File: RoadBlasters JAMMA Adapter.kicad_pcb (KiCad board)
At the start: 2 copper layers, 112.2 x 82 mm, 44 parts, among them J101 Molex_KK-396_5273-10A_1x10_P3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, J102 Molex_KK-254_AE-6410-02A_1x02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, J103 Molex_KK-254_AE-6410-02A_1x02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, J104 Molex_KK-254_AE-6410-02A_1x02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, J105 Molex_KK-254_AE-6410-04A_1x04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, J106 Molex_KK-254_AE-6410-03A_1x03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, J108 Molex_KK-254_AE-6410-05A_1x05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, P1 10K, U1 74LS86, U2 NE555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

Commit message: 152 changed to 2a152j (reduced noise), other tweaks
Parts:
- C10: value 152 -> 2A152J
- U1: footprint Package_DIP:DIP-14_W7.62mm_Socket -> Package_DIP:DIP-14_W7.62mm
- moved C7 0.25 mm to (134.2, 99.0)
- moved C11 0.20 mm to (121.1, 77.2)
- moved U2 0.18 mm to (134.4, 82.4)
- moved U1 0.16 mm to (121.0, 82.4)
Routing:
- net +5V: track 472.7 -> 473.8 mm
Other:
- board text added: "Atari® System I JAMMA Interface, Rev. 1 for RoadBlasters®"
- board text removed: "Atari® System I JAMMA Interface for RoadBlasters®, Rev. 1"

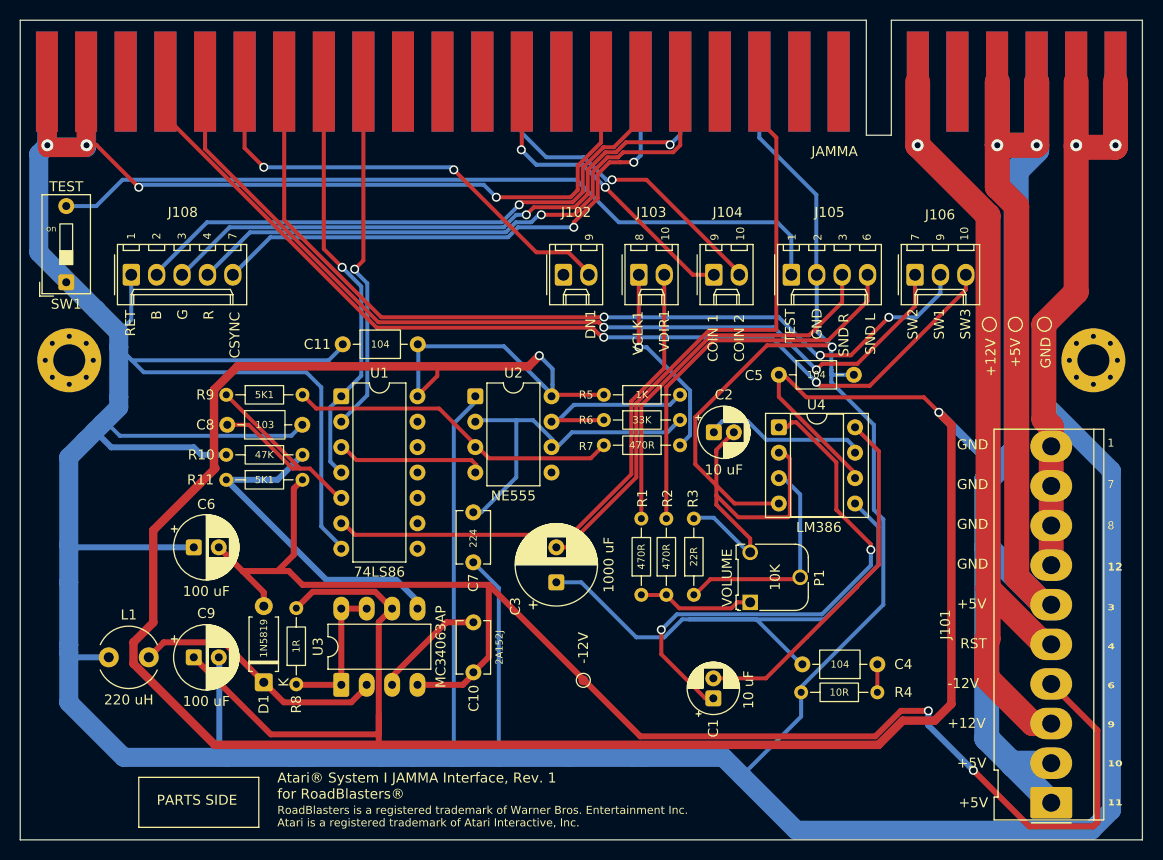
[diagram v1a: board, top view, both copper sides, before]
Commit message: add jumper to select button 2 behavior: gas or brake
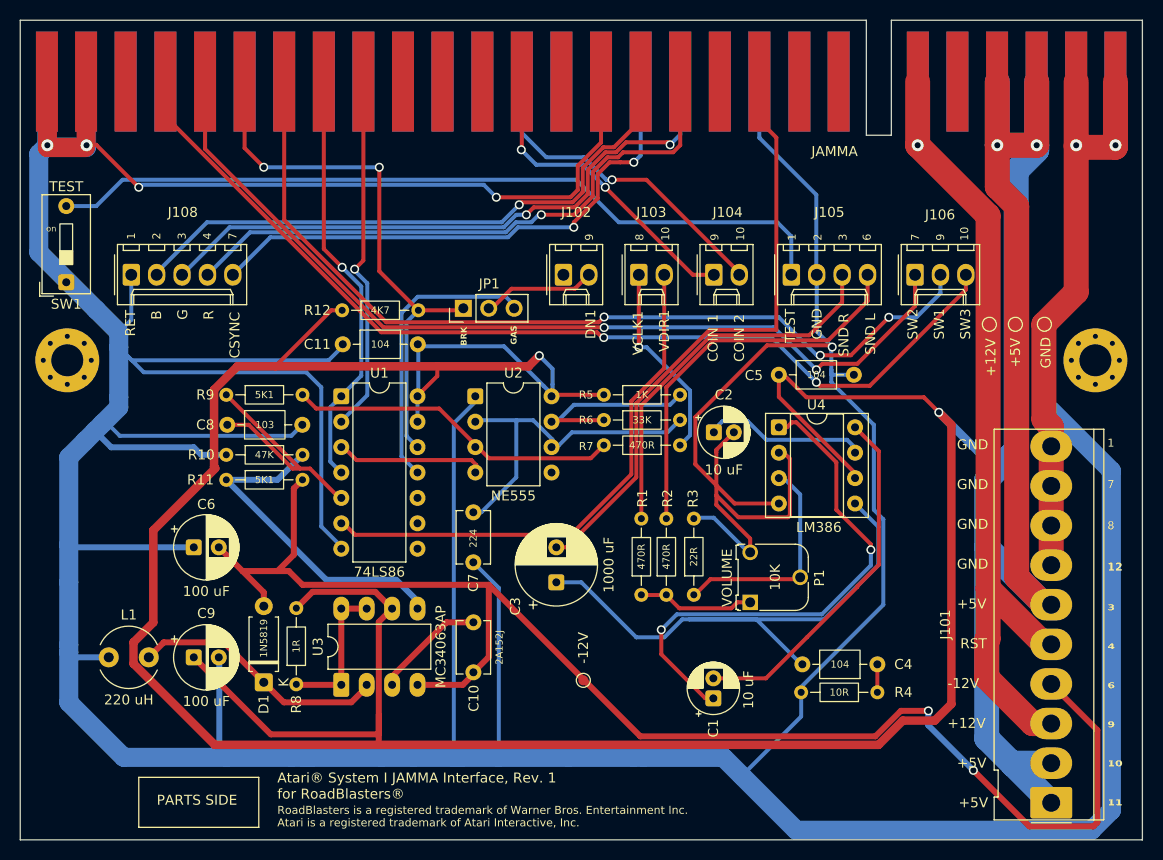
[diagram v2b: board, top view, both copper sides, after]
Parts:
- added JP1: PinHeader_1x03_P2.54mm_Vertical, Connector_PinHeader_2.54mm:PinHeader_1x03_P2.54mm_Vertical, F.Cu at (133.2, 73.6)
- added R12: 4K7, Resistor_THT:R_Axial_DIN0204_L3.6mm_D1.6mm_P7.62mm_Horizontal, F.Cu at (121.1, 73.8)
- moved PMH1 0.20 mm to (196.4, 78.8)
- moved PMH4 0.20 mm to (93.6, 78.8)
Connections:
- J102 pad 2: 1P_B2 -> 1P_B2_OUT
- U1 pad 11: (no net) -> !1P_B2
- U1 pad 12: (no net) -> 1P_B2
- U1 pad 13: (no net) -> +5V
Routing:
- net !1P_B2: track 0.00 -> 29.2 mm
- net +5V: track 473.8 -> 485.3 mm
- net 1P_B2_OUT: track 0.00 -> 11.4 mm
- net 1P_B2: track 46.2 -> 56.2 mm
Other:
- board text added: "BRK"
- board text added: "GAS"

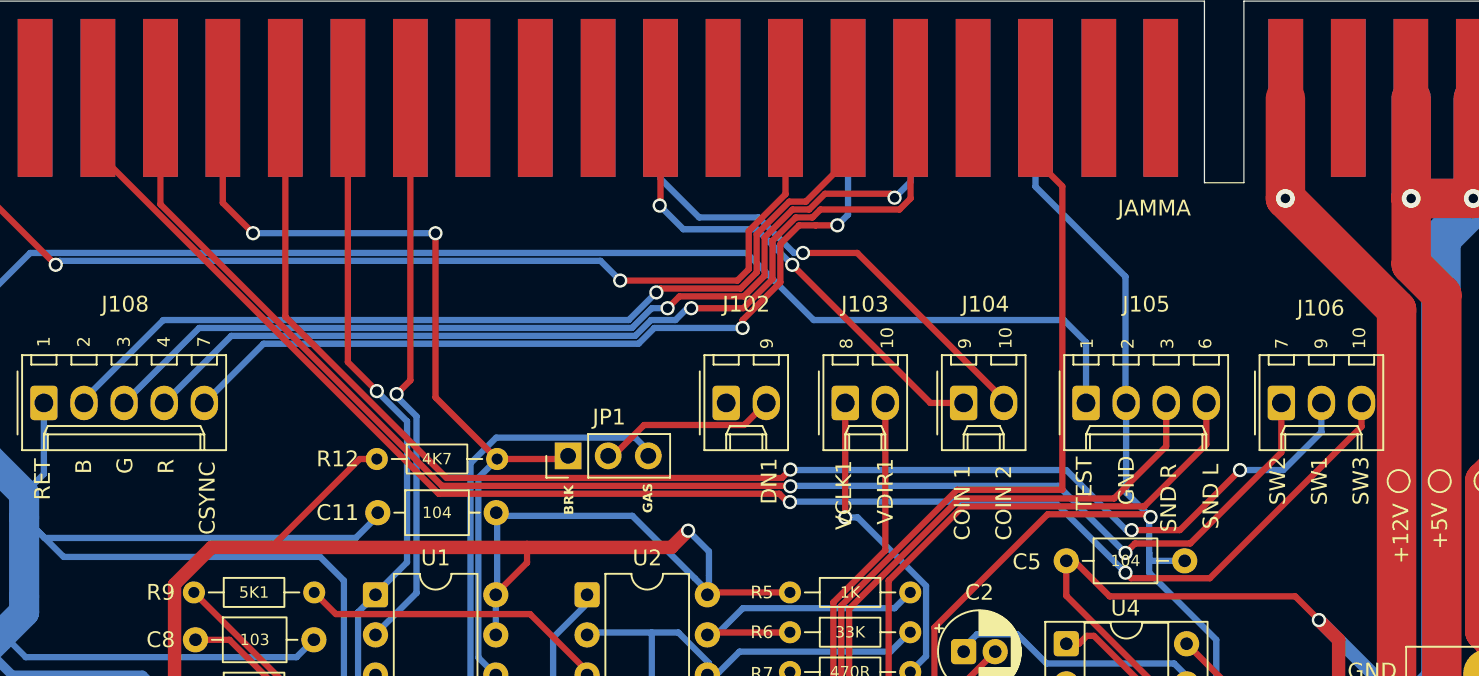
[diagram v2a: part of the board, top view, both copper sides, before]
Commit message: eliminate SW3 connection
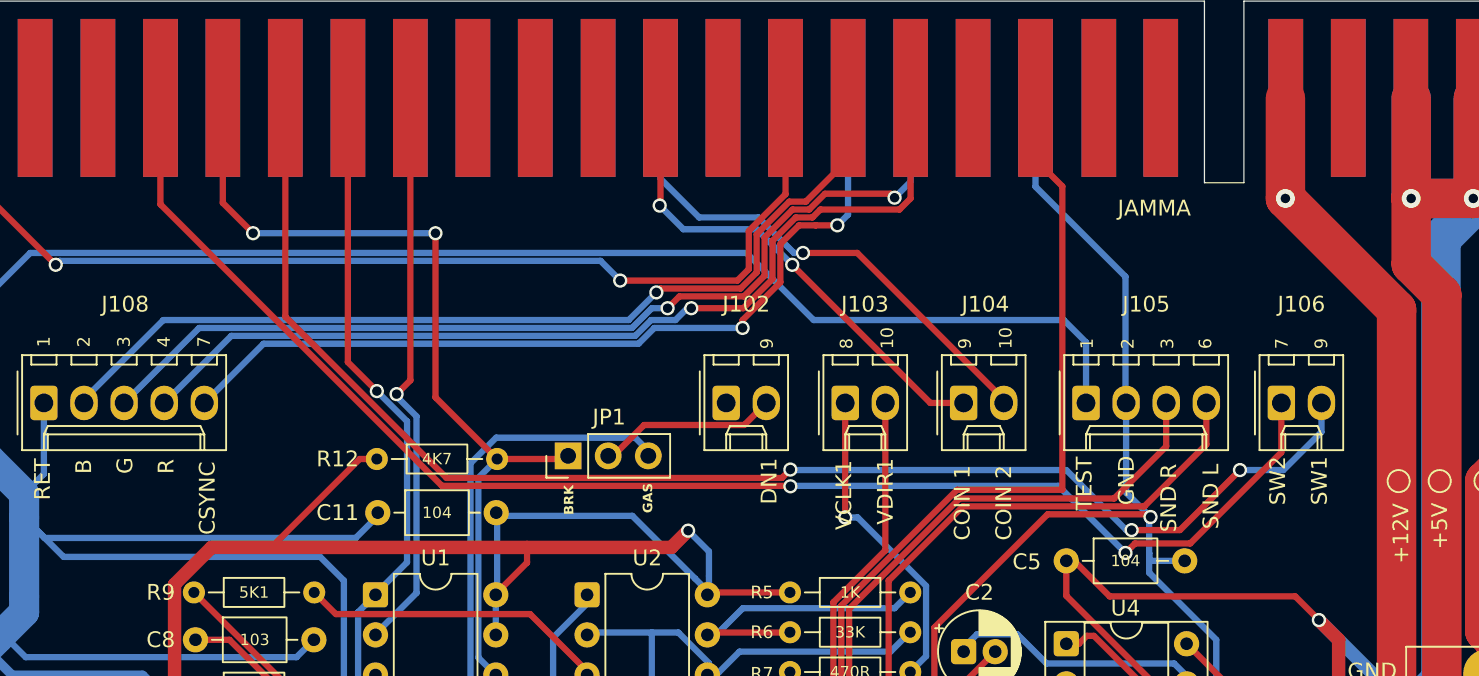
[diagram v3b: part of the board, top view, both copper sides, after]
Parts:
- J106: value Molex_KK-254_AE-6410-03A_1x03_P2.54mm_Vertical -> Molex_KK-254_AE-6410-02A_1x02_P2.54mm_Vertical; footprint Connector_Molex:Molex_KK-254_AE-6410-03A_1x03_P2.54mm_Vertical -> Connector_Molex:Molex_KK-254_AE-6410-02A_1x02_P2.54mm_Vertical
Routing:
- net 1P_B4: track 100.2 -> 0.00 mm, vias 2 -> 0
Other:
- board text removed: "SW3"
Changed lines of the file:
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@@
 		)
 	)
-	(footprint "Connector_Molex:Molex_KK-254_AE-6410-03A_1x03_P2.54mm_Vertical"
+	(footprint "Connector_Molex:Molex_KK-254_AE-6410-02A_1x02_P2.54mm_Vertical"
 		(layer "F.Cu")
 		(at 178.36937 70.25)
-		(descr "Molex KK-254 Interconnect System, old/engineering part number: AE-6410-03A example for new part number: 22-27-2031, 3 Pins (http://www.molex.com/pdm_docs/sd/022272021_sd.pdf), generated with kicad-footprint-generator")
+		(descr "Molex KK-254 Interconnect System, old/engineering part number: AE-6410-02A example for new part number: 22-27-2021, 2 Pins (http://www.molex.com/pdm_docs/sd/022272021_sd.pdf), generated with kicad-footprint-generator")
 		(tags "connector Molex KK-254 vertical")
 		(property "Reference" "J106"
-			(at 2.5 -6 0)
+			(at 1.27 -6.25 0)
 			(layer "F.SilkS" knockout)
 			(effects
@@
 			)
 		)
-		(property "Value" "Molex_KK-254_AE-6410-03A_1x03_P2.54mm_Vertical"
-			(at 2.54 4.08 0)
+		(property "Value" "Molex_KK-254_AE-6410-02A_1x02_P2.54mm_Vertical"
+			(at 1.27 4.08 0)
 			(layer "F.Fab")
 			(hide yes)
@@
 		(fp_line
 			(start -1.38 2.99)
-			(end 6.46 2.99)
+			(end 3.92 2.99)
 			(stroke
 				(width 0.12)
@@
 		(fp_line
 			(start 0 1.99)
-			(end 5.08 1.99)
+			(end 2.54 1.99)
 			(stroke
 				(width 0.12)
@@
 		(fp_line
 			(start 0.25 1.46)
-			(end 4.83 1.46)
+			(end 2.29 1.46)
 			(stroke
 				(width 0.12)
@@
 		)
 		(fp_line
-			(start 3.34 -2.43)
-			(end 3.34 -3.03)
-			(stroke
-				(width 0.12)
-				(type solid)
-			)
-			(layer "F.SilkS")
-		)
-		(fp_line
-			(start 4.28 -3.03)
-			(end 4.28 -2.43)
-			(stroke
-				(width 0.12)
-				(type solid)
-			)
-			(layer "F.SilkS")
-		)
-		(fp_line
-			(start 4.28 -2.43)
-			(end 5.88 -2.43)
-			(stroke
-				(width 0.12)
-				(type solid)
-			)
-			(layer "F.SilkS")
-		)
-		(fp_line
-			(start 4.83 1.46)
-			(end 5.08 1.99)
+			(start 2.29 1.46)
+			(end 2.54 1.99)
 			(stroke
 				(width 0.12)
@@
 		)
 		(fp_line
-			(start 4.83 2.99)
-			(end 4.83 1.99)
+			(start 2.29 2.99)
+			(end 2.29 1.99)
 			(stroke
 				(width 0.12)
@@
 		)
 		(fp_line
-			(start 5.08 1.99)
-			(end 5.08 2.99)
+			(start 2.54 1.99)
+			(end 2.54 2.99)
 			(stroke
 				(width 0.12)
@@
 		)
 		(fp_line
-			(start 5.88 -2.43)
-			(end 5.88 -3.03)
+			(start 3.34 -2.43)
+			(end 3.34 -3.03)
 			(stroke
 				(width 0.12)
@@
 		)
 		(fp_line
-			(start 6.46 -3.03)
+			(start 3.92 -3.03)
 			(end -1.38 -3.03)
 			(stroke
@@
 		)
 		(fp_line
-			(start 6.46 2.99)
-			(end 6.46 -3.03)
+			(start 3.92 2.99)
+			(end 3.92 -3.03)
 			(stroke
 				(width 0.12)
@@
 		(fp_line
 			(start -1.77 3.38)
-			(end 6.85 3.38)
+			(end 4.32 3.38)
 			(stroke
 				(width 0.05)
@@
 		)
 		(fp_line
-			(start 6.85 -3.42)
+			(start 4.32 -3.42)
 			(end -1.77 -3.42)
 			(stroke
@@
 		)
 		(fp_line
-			(start 6.85 3.38)
-			(end 6.85 -3.42)
+			(start 4.32 3.38)
+			(end 4.32 -3.42)
 			(stroke
 				(width 0.05)
@@
 		(fp_line
 			(start -1.27 2.88)
-			(end 6.35 2.88)
+			(end 3.81 2.88)
 			(stroke
 				(width 0.1)
@@
 		)
 		(fp_line
-			(start 6.35 -2.92)
+			(start 3.81 -2.92)
 			(end -1.27 -2.92)
 			(stroke
@@
 		)
 		(fp_line
-			(start 6.35 2.88)
-			(end 6.35 -2.92)
+			(start 3.81 2.88)
+			(end 3.81 -2.92)
 			(stroke
 				(width 0.1)
@@
 		)
 		(fp_text user "${REFERENCE}"
-			(at 2.54 -2.22 0)
+			(at 1.27 -2.22 0)
 			(layer "F.Fab")
 			(effects
@@
 			(net 14 "1P_B1")
 		)
-		(pad "3" thru_hole oval
-			(at 5.08 0)
-			(size 1.74 2.19)
-			(drill 1.19)
-			(layers "*.Cu" "*.Mask")
-			(remove_unused_layers no)
-			(net 35 "1P_B4")
-		)
 		(embedded_fonts no)
-		(model "${KICAD9_3DMODEL_DIR}/Connector_Molex.3dshapes/Molex_KK-254_AE-6410-03A_1x03_P2.54mm_Vertical.step"
+		(model "${KICAD9_3DMODEL_DIR}/Connector_Molex.3dshapes/Molex_KK-254_AE-6410-02A_1x02_P2.54mm_Vertical.step"
 			(offset
 				(xyz 0 0 0)
@@
 		)
 	)
-	(gr_text "SW3"
-		(at 184 76.72619 90)
-		(layer "F.SilkS")
-		(effects
-			(font
-				(size 1 1)
-				(thickness 0.15)
-			)
-			(justify left bottom)
-		)
-	)
 	(gr_text "9"
 		(at 146.259071 66.83894 90)
@@
 		)
 	)
-	(gr_text "10"
-		(at 183.778036 66.83894 90)
-		(layer "F.SilkS")
-		(effects
-			(font
-				(size 0.8 0.8)
-				(thickness 0.15)
-			)
-			(justify left bottom)
-		)
-	)
 	(gr_text "7"
 		(at 178.86937 66.83894 90)
@@
 	)
 	(segment
-		(start 183.44937 71.745)
-		(end 173.84337 81.351)
-		(width 0.4)
-		(layer "F.Cu")
-		(net 35)
-	)
-	(segment
-		(start 146.575 76)
-		(end 147.102509 76.527509)
-		(width 0.4)
-		(layer "F.Cu")
-		(net 35)
-	)
-	(segment
-		(start 168.851 81.351)
-		(end 168.5 81)
-		(width 0.4)
-		(layer "F.Cu")
-		(net 35)
-	)
-	(segment
-		(start 147.102509 76.527509)
-		(end 147.249202 76.527509)
-		(width 0.4)
-		(layer "F.Cu")
-		(net 35)
-	)
-	(segment
-		(start 103.42 50.930005)
-		(end 103.42 54.42)
-		(width 0.4)
-		(layer "F.Cu")
-		(net 35)
-	)
-	(segment
-		(start 173.84337 81.351)
-		(end 168.851 81.351)
-		(width 0.4)
-		(layer "F.Cu")
-		(net 35)
-	)
-	(segment
-		(start 183.44937 70.25)
-		(end 183.44937 71.745)
-		(width 0.4)
-		(layer "F.Cu")
-		(net 35)
-	)
-	(segment
-		(start 125 76)
-		(end 146.575 76)
-		(width 0.4)
-		(layer "F.Cu")
-		(net 35)
-	)
-	(segment
-		(start 103.42 54.42)
-		(end 125 76)
-		(width 0.4)
-		(layer "F.Cu")
-		(net 35)
-	)
-	(via
-		(at 168.5 81)
-		(size 0.9)
-		(drill 0.6)
-		(layers "F.Cu" "B.Cu")
-		(net 35)
-	)
-	(via
-		(at 147.249202 76.527509)
-		(size 0.9)
-		(drill 0.6)
-		(layers "F.Cu" "B.Cu")
-		(net 35)
-	)
-	(segment
-		(start 147.276711 76.5)
-		(end 147.249202 76.527509)
-		(width 0.4)
-		(layer "B.Cu")
-		(net 35)
-	)
-	(segment
-		(start 164 76.5)
-		(end 147.276711 76.5)
-		(width 0.4)
-		(layer "B.Cu")
-		(net 35)
-	)
-	(segment
-		(start 168.5 81)
-		(end 164 76.5)
-		(width 0.4)
-		(layer "B.Cu")
-		(net 35)
-	)
-	(segment
